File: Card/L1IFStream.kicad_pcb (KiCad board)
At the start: 4 copper layers, 88.9 x 50.8 mm, 109 parts, among them J1 Conn_Coaxial, J2 USB_A, J3 RF_Shield_One_Piece, J4 Conn_Coaxial, U1 MAX2769ETI+T, U10 74LVC374, U11 74HC2GU04, U2 TPS717285DCKR, U3 TPS717285DCKR, U4 NCP164CSN330T1G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

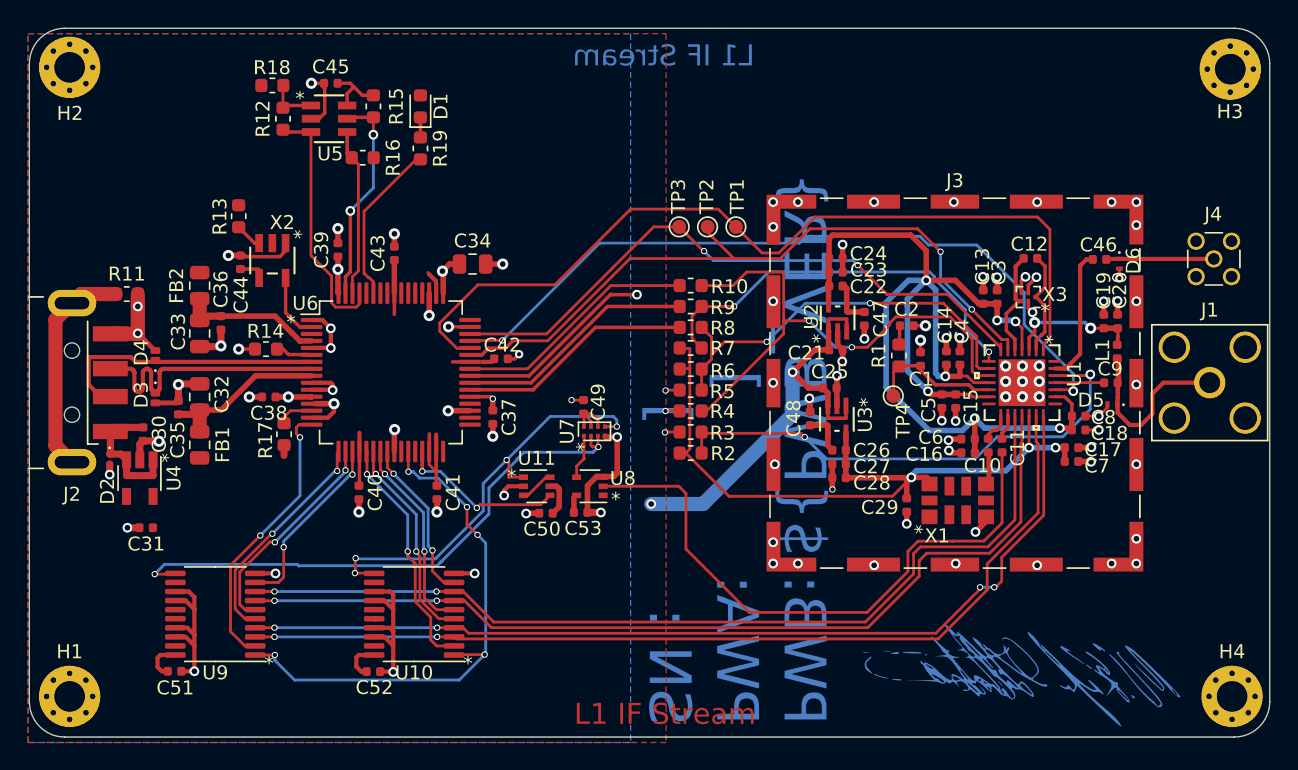
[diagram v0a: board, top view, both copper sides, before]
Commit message: Squared up L1IFTHMB and L1IFStream to implement the same nibble selector
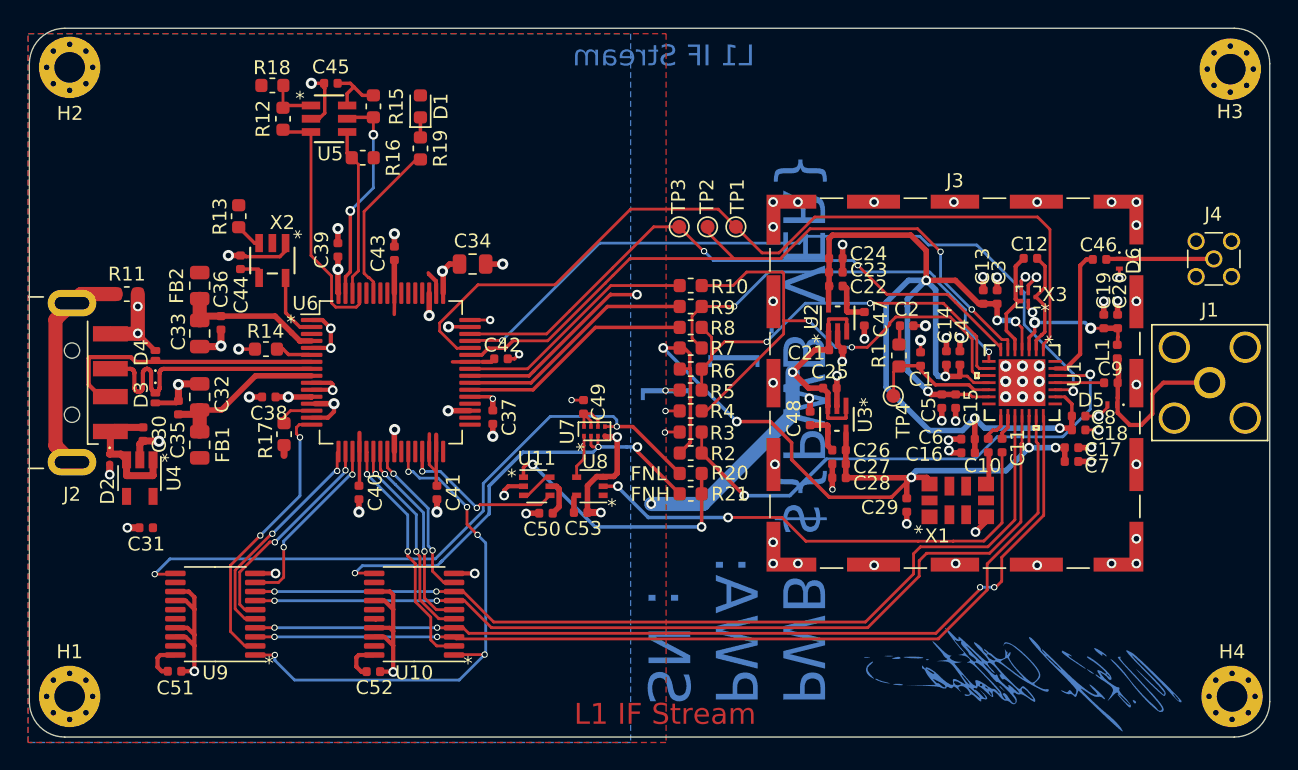
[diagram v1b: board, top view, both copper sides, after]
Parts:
- added R20: NL, L1IFStream:R_0603_1608Metric, F.Cu at (137.2, 104.7)
- added R21: 0, L1IFStream:R_0603_1608Metric, F.Cu at (137.2, 106.1)
- moved G*** 0.36 mm to (163.3, 120.5)
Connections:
- U10 pad 11: /CLKOUT2 -> /~{CLKOUT2}
- U11 pad 1: /CLKOUT2 -> Net-(U11A-1A)
- U6 pad 48: unconnected-(U6-BCBUS0-Pad48) -> /BCBUS0
- U9 pad 11: /~{CLKOUT2} -> /CLKOUT2
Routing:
- net Net-(U11A-1A): track 0.00 -> 19.4 mm, vias 0 -> 2
- net /CLKOUT2: track 30.3 -> 47.8 mm, vias 4 -> 2
- net /CLKOUT: track 43.2 -> 35.9 mm, vias 0 -> 2
- net /~{CLKOUT2}: track 40.5 -> 33.4 mm, vias 2 -> 3
- net /2V85D: track 53.8 -> 60.1 mm, vias 3 -> 5
- net /PGM: track 36.6 -> 38.2 mm
- net /BCBUS0: track 0.00 -> 1.45 mm, vias 0 -> 1
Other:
- board text added: "FNH"
- board text added: "FNL"

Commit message: Started cleaning up symbol library
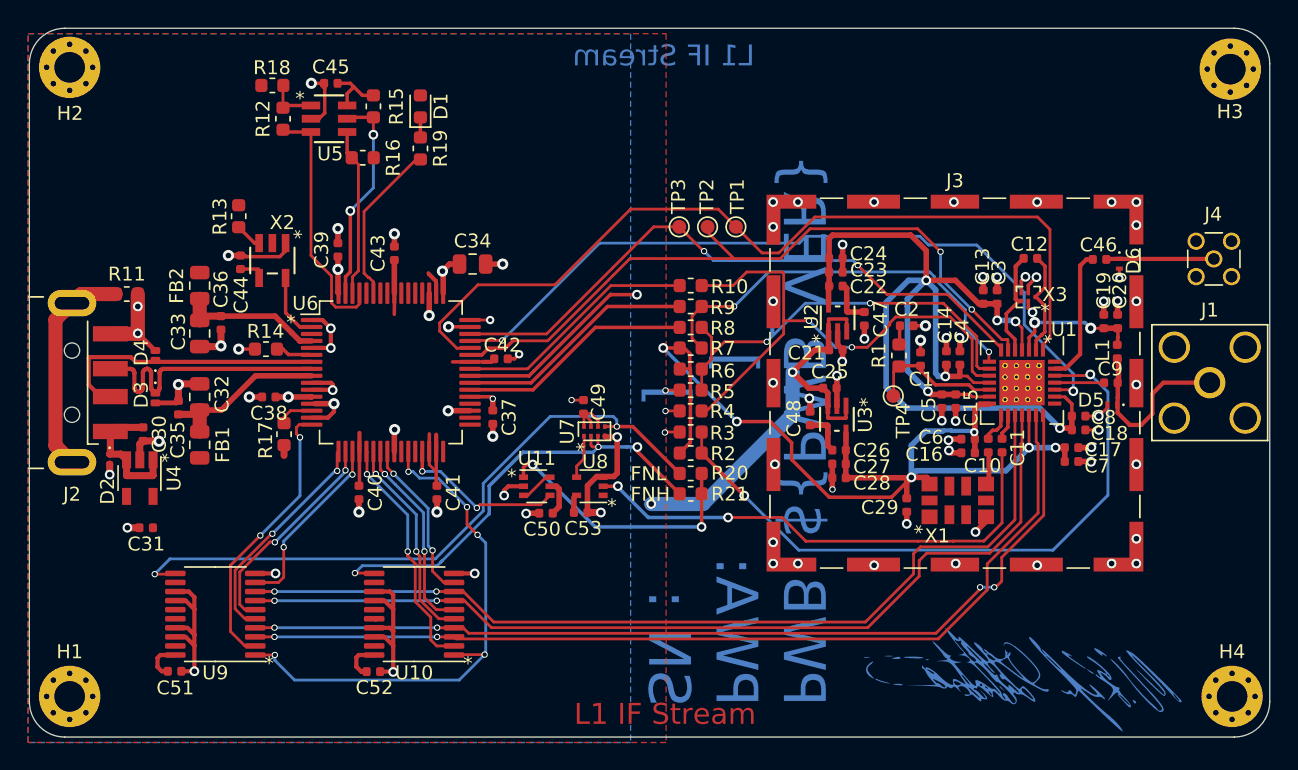
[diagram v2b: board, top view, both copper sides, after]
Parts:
- U1: value MAX2769ETI+T -> MAX2769BETI+T; footprint L1IFStream:MAX2769ETI&plus_T -> L1IF:QFN-28_EP_5.63x5.63_Pitch0.5mm
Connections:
- C16 pad 1: /2V85A -> /2V85D
- C6 pad 1: /2V85A -> /2V85D
- U1 pad 14: /2V85A -> /2V85D
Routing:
- net /2V85D: track 60.1 -> 71.8 mm, vias 5 -> 6
- net /PGM: track 38.2 -> 46.9 mm
- net /2V85A: track 82.4 -> 79.2 mm, vias 7 -> 6
- net GND: vias 99 -> 90

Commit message: Library clean up of oscillators and U1
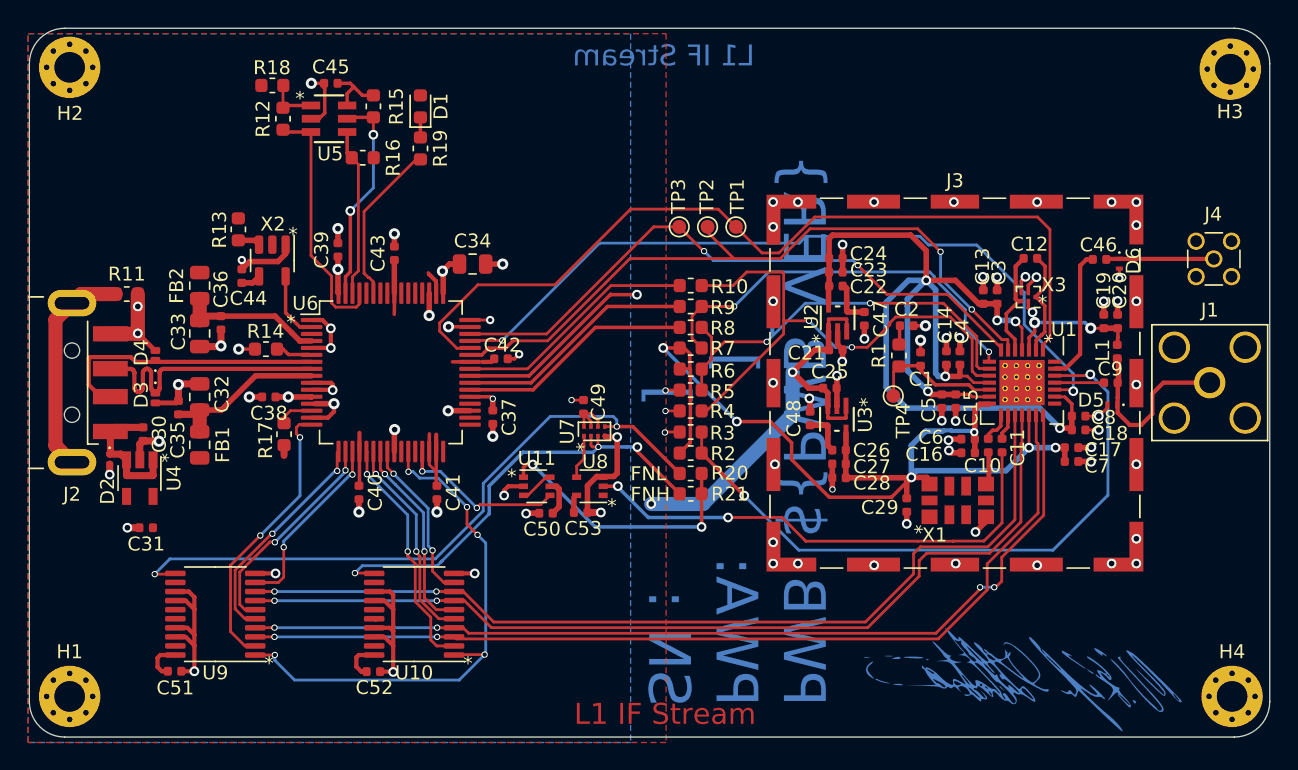
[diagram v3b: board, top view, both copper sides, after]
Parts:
- X1: footprint L1IFStream:10L_CQFN -> L1IF:10L_CQFN
- X2: value SIT2024BA-S8-33E-12.00000E -> SiT2024B; footprint L1IFStream:SIT2024BA-S8-33E-12.000000E -> L1IF:SOT-23-5
- X3: footprint L1IFStream:QPQ1060_1.4x1.2 -> L1IF:QPQ1060_1.4x1.2
- moved C44 0.99 mm to (105.0, 90.5)
- moved R13 0.94 mm to (104.8, 87.2)
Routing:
- net GND: track 136.1 -> 136.7 mm

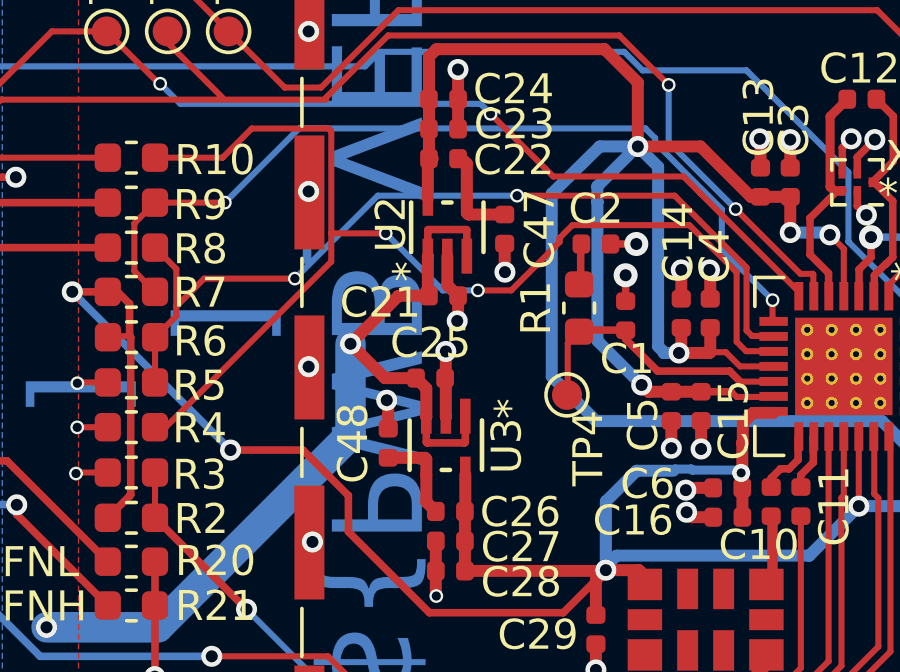
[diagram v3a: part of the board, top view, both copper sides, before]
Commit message: Cleaned up library through U3
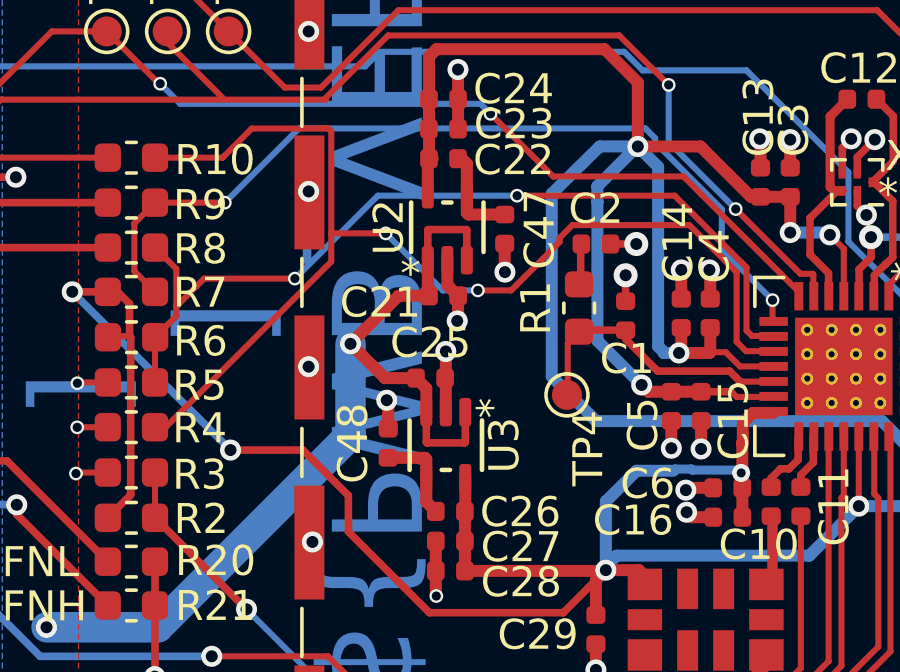
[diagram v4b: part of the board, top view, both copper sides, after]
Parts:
- U2, U3: value TPS717285DCKR -> TPS717285DCK; footprint L1IFStream:TPS717285DCKR -> L1IF:TPS717285DCK
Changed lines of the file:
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@@
     )
   )
-  (footprint "L1IFStream:TPS717285DCKR" (layer "F.Cu")
+  (footprint "L1IF:TPS717285DCK" (layer "F.Cu")
     (at 147.752 93.523 90)
     (property "Description" "IC REG LINEAR 2.85V 150MA SC70-5")
-    (property "MPN" "TPS717285DCKR")
+    (property "MPN" "TPS717285DCK")
     (property "Manufacturer" "Texas Instruments")
     (property "Sheetfile" "L1IFStream.kicad_sch")
     (property "Sheetname" "")
     (property "Vendor" "DigiKey")
-    (property "Vendor P/N#" "296-19649-1-ND")
+    (property "Vendor PN" "296-32541-6-ND")
     (attr through_hole)
-    (fp_text reference "U2" (at 0.1018 -1.8798 90) (layer "F.SilkS")
+    (fp_text reference "U2" (at 0 -1.95 90) (layer "F.SilkS")
         (effects (font (size 1 1) (thickness 0.15)))
     )
-    (fp_text value "TPS717285DCKR" (at 0 0 90) (layer "F.Fab")
+    (fp_text value "TPS717285DCK" (at 0 0 90) (layer "F.SilkS") hide
         (effects (font (size 1 1) (thickness 0.15)))
     )
-    (fp_text user "*" (at -1.473 -1.2956 90) (layer "F.SilkS")
+    (fp_text user "*" (at -1.552 -1.227) (layer "F.SilkS")
         (effects (font (size 1 1) (thickness 0.15)))
     )
-    (fp_text user "Copyright 2016 Accelerated Designs. All rights reserved." (at 0 0 90) (layer "Cmts.User")
-        (effects (font (size 0.127 0.127) (thickness 0.002)))
-    )
-    (fp_text user "*" (at -1.5 -1.1834 90) (layer "F.Fab")
+    (fp_text user "${REFERENCE}" (at -0.4445 -1.1834 90) (layer "F.Fab")
         (effects (font (size 1 1) (thickness 0.15)))
     )
@@
     (fp_arc (start 0.3048 -1.0795) (mid 0 -0.7747) (end -0.3048 -1.0795)
       (stroke (width 0.1524) (type solid)) (layer "F.Fab"))
-    (pad "1" smd rect (at -0.9652 -0.649999 90) (size 1.1684 0.3556) (layers "F.Cu" "F.Paste" "F.Mask")
+    (pad "1" smd roundrect (at -1.1 -0.649999 90) (size 0.95 0.4) (layers "F.Cu" "F.Paste" "F.Mask") (roundrect_rratio 0.25)
       (net 21 "+3V3") (pinfunction "IN") (pintype "input"))
-    (pad "2" smd rect (at -0.9652 0 90) (size 1.1684 0.3556) (layers "F.Cu" "F.Paste" "F.Mask")
+    (pad "2" smd roundrect (at -1.1 0 90) (size 0.95 0.4) (layers "F.Cu" "F.Paste" "F.Mask") (roundrect_rratio 0.25)
       (net 4 "GND") (pinfunction "GND") (pintype "power_in"))
-    (pad "3" smd rect (at -0.9652 0.649999 90) (size 1.1684 0.3556) (layers "F.Cu" "F.Paste" "F.Mask")
+    (pad "3" smd roundrect (at -1.1 0.649999 90) (size 0.95 0.4) (layers "F.Cu" "F.Paste" "F.Mask") (roundrect_rratio 0.25)
       (net 21 "+3V3") (pinfunction "EN") (pintype "unspecified"))
-    (pad "4" smd rect (at 0.9652 0.649999 90) (size 1.1684 0.3556) (layers "F.Cu" "F.Paste" "F.Mask")
+    (pad "4" smd roundrect (at 1.1 0.649999 90) (size 0.95 0.4) (layers "F.Cu" "F.Paste" "F.Mask") (roundrect_rratio 0.25)
       (net 8 "Net-(U2-NR{slash}FB)") (pinfunction "NR/FB") (pintype "bidirectional"))
-    (pad "5" smd rect (at 0.9652 -0.649999 90) (size 1.1684 0.3556) (layers "F.Cu" "F.Paste" "F.Mask")
+    (pad "5" smd roundrect (at 1.1 -0.649999 90) (size 0.95 0.4) (layers "F.Cu" "F.Paste" "F.Mask") (roundrect_rratio 0.25)
       (net 23 "/2V85A") (pinfunction "OUT") (pintype "output"))
-    (model "${KIPRJMOD}/STEP/SOT-23-5.step"
+    (model "${KIPRJMOD}/STEP/DCK0005A.stp"
       (offset (xyz 0 0 0))
       (scale (xyz 1 1 1))
@@
     (pad "10" smd rect (at 0 -2.025 90) (size 0.7 1.15) (layers "F.Cu" "F.Paste" "F.Mask")
       (net 94 "unconnected-(X1-NC-Pad10)") (pinfunction "NC") (pintype "no_connect"))
+    (model "${KIPRJMOD}/STEP/Oscillator_SMD_IDT_JS6-6_5.0x3.2mm_P1.27mm.step"
+      (offset (xyz 0 0 0))
+      (scale (xyz 1 1 1))
+      (rotate (xyz 0 0 0))
+    )
   )
   (footprint "L1IF:QPQ1060_1.4x1.2" (layer "F.Cu")
@@
     )
   )
-  (footprint "L1IFStream:TPS717285DCKR" (layer "F.Cu")
+  (footprint "L1IF:TPS717285DCK" (layer "F.Cu")
     (at 147.701 100.7872 -90)
     (property "Description" "IC REG LINEAR 2.85V 150MA SC70-5")
-    (property "MPN" "TPS717285DCKR")
+    (property "MPN" "TPS717285DCK")
     (property "Manufacturer" "Texas Instruments")
     (property "Sheetfile" "L1IFStream.kicad_sch")
     (property "Sheetname" "")
     (property "Vendor" "DigiKey")
-    (property "Vendor P/N#" "296-19649-1-ND")
+    (property "Vendor PN" "296-32541-6-ND")
     (attr through_hole)
-    (fp_text reference "U3" (at 0.0254 -2.032 90) (layer "F.SilkS")
-        (effects (font (size 1 1) (thickness 0.15)))
-    )
-    (fp_text value "TPS717285DCKR" (at 0 0 90) (layer "F.SilkS") hide
+    (fp_text reference "U3" (at 0 -1.95 -90) (layer "F.SilkS")
         (effects (font (size 1 1) (thickness 0.15)))
     )
-    (fp_text user "*" (at -1.2192 -2.1486 90) (layer "F.SilkS")
+    (fp_text value "TPS717285DCK" (at 0 0 -90) (layer "F.SilkS") hide
         (effects (font (size 1 1) (thickness 0.15)))
     )
-    (fp_text user "*" (at -1.2192 -2.1486 90) (layer "F.SilkS")
+    (fp_text user "*" (at -1.2372 -1.549 -90) (layer "F.SilkS")
         (effects (font (size 1 1) (thickness 0.15)))
     )
-    (fp_text user "Copyright 2016 Accelerated Designs. All rights reserved." (at 0 0 90) (layer "Cmts.User") hide
-        (effects (font (size 0.127 0.127) (thickness 0.002)))
-    )
-    (fp_text user "*" (at -0.4445 -1.1834 90) (layer "F.Fab")
+    (fp_text user "*" (at -0.4445 -1.1834 -90) (layer "F.Fab")
         (effects (font (size 1 1) (thickness 0.15)))
     )
-    (fp_text user "*" (at -0.4445 -1.1834 90) (layer "F.Fab")
+    (fp_text user "${REFERENCE}" (at -0.4445 -1.1834 -90) (layer "F.Fab")
         (effects (font (size 1 1) (thickness 0.15)))
     )
@@
     (fp_arc (start 0.3048 -1.0795) (mid 0 -0.7747) (end -0.3048 -1.0795)
       (stroke (width 0.1524) (type solid)) (layer "F.Fab"))
-    (pad "1" smd rect (at -0.9652 -0.649999 270) (size 1.1684 0.3556) (layers "F.Cu" "F.Paste" "F.Mask")
+    (pad "1" smd roundrect (at -1.1 -0.649999 270) (size 0.95 0.4) (layers "F.Cu" "F.Paste" "F.Mask") (roundrect_rratio 0.25)
       (net 21 "+3V3") (pinfunction "IN") (pintype "input"))
-    (pad "2" smd rect (at -0.9652 0 270) (size 1.1684 0.3556) (layers "F.Cu" "F.Paste" "F.Mask")
+    (pad "2" smd roundrect (at -1.1 0 270) (size 0.95 0.4) (layers "F.Cu" "F.Paste" "F.Mask") (roundrect_rratio 0.25)
       (net 4 "GND") (pinfunction "GND") (pintype "power_in"))
-    (pad "3" smd rect (at -0.9652 0.649999 270) (size 1.1684 0.3556) (layers "F.Cu" "F.Paste" "F.Mask")
+    (pad "3" smd roundrect (at -1.1 0.649999 270) (size 0.95 0.4) (layers "F.Cu" "F.Paste" "F.Mask") (roundrect_rratio 0.25)
       (net 21 "+3V3") (pinfunction "EN") (pintype "unspecified"))
-    (pad "4" smd rect (at 0.9652 0.649999 270) (size 1.1684 0.3556) (layers "F.Cu" "F.Paste" "F.Mask")
+    (pad "4" smd roundrect (at 1.1 0.649999 270) (size 0.95 0.4) (layers "F.Cu" "F.Paste" "F.Mask") (roundrect_rratio 0.25)
       (net 9 "Net-(U3-NR{slash}FB)") (pinfunction "NR/FB") (pintype "bidirectional"))
-    (pad "5" smd rect (at 0.9652 -0.649999 270) (size 1.1684 0.3556) (layers "F.Cu" "F.Paste" "F.Mask")
+    (pad "5" smd roundrect (at 1.1 -0.649999 270) (size 0.95 0.4) (layers "F.Cu" "F.Paste" "F.Mask") (roundrect_rratio 0.25)
       (net 24 "/2V85D") (pinfunction "OUT") (pintype "output"))
+    (model "${KIPRJMOD}/STEP/DCK0005A.stp"
+      (offset (xyz 0 0 0))
+      (scale (xyz 1 1 1))
+      (rotate (xyz 0 0 0))
+    )
   )
   (footprint "L1IFStream:SOT-353_SC-70-5" (layer "F.Cu")
